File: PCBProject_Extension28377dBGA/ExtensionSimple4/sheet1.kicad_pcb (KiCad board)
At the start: 4 copper layers, 153.2 x 142.2 mm, 353 parts, among them J1 Conn_02x05_Odd_Even, J2 Conn_02x05_Odd_Even, J3 Conn_02x05_Odd_Even, J4 Conn_02x05_Odd_Even, Q1 FMMT618TA, U1 SN74ABT541, U2 SN74ABT541, U3 SN74ABT541, U4 SN74ABT541, U5 ADR423ARZ

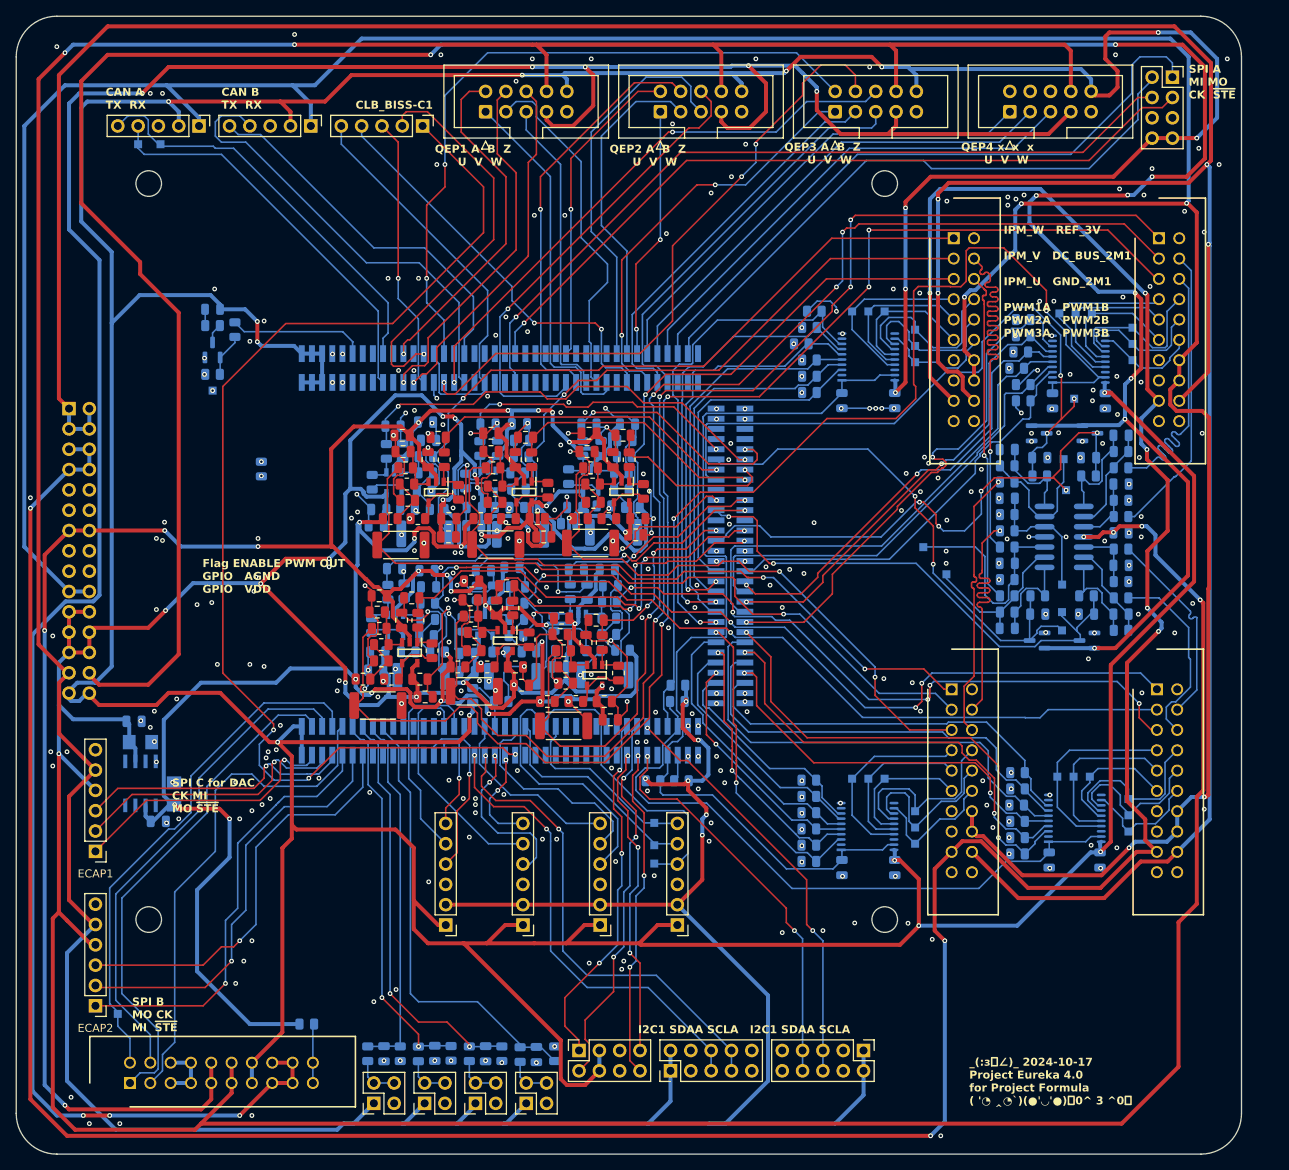
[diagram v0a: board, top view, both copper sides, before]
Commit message: waiting for improving quality of current sensor signals
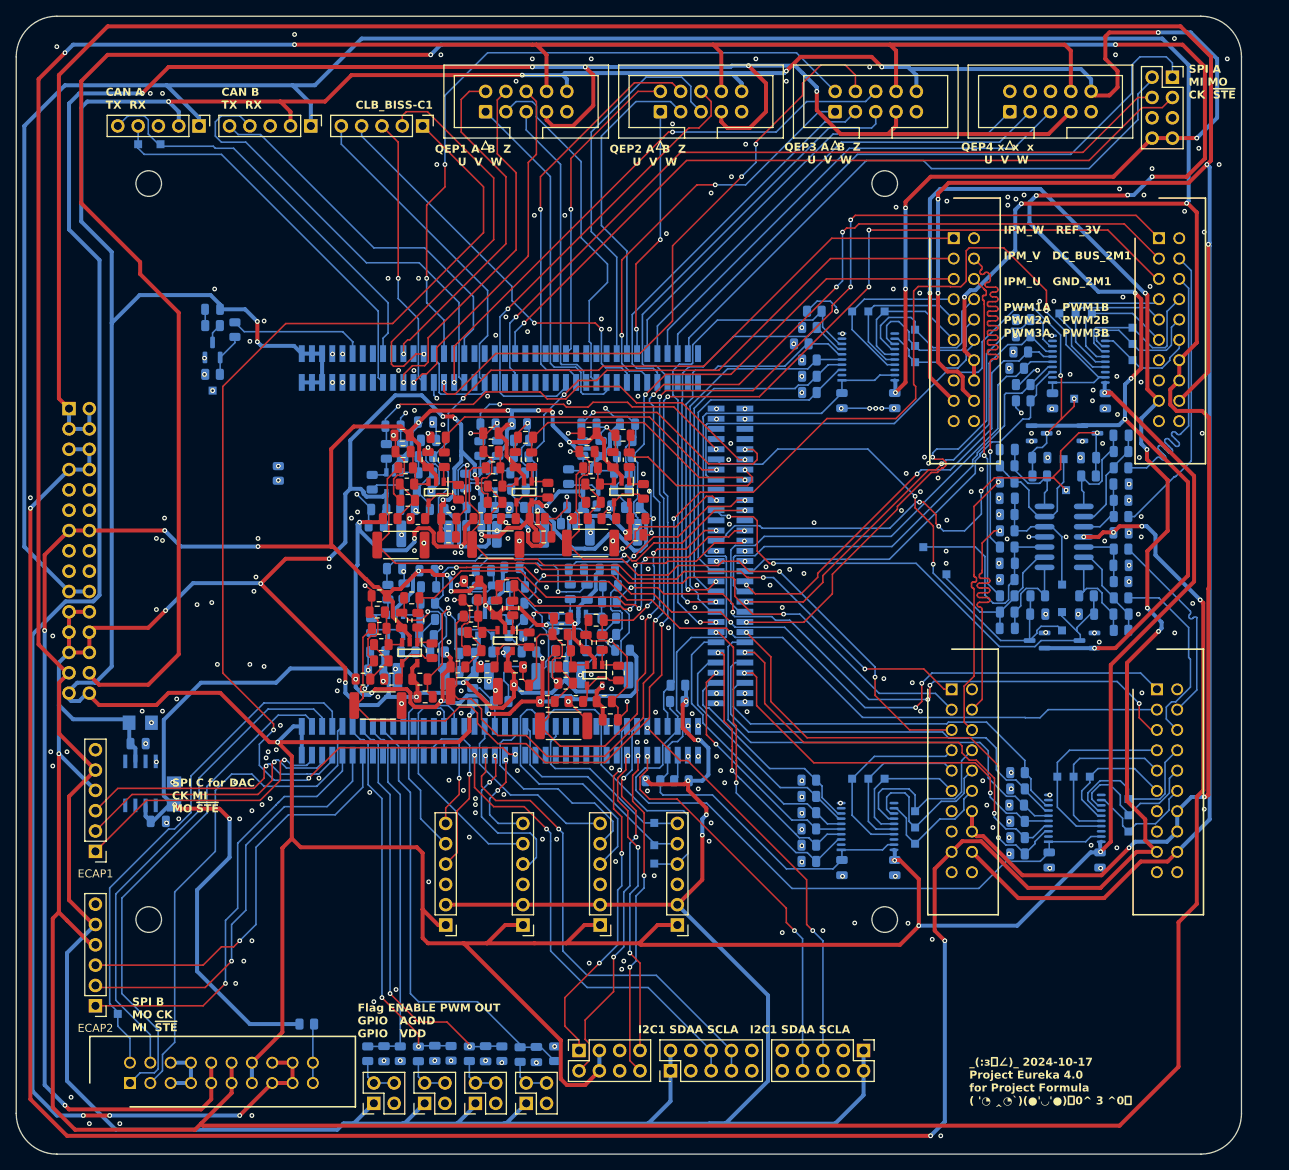
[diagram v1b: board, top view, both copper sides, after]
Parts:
- moved C23 2.84 mm to (190.0, 136.7)
- moved C25 2.43 mm to (188.9, 134.0)
- moved RU1 2.19 mm to (207.5, 102.9)
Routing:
- net REF_3V: track 249.8 -> 247.3 mm
- net D+5V: track 731.3 -> 729.3 mm
- net /IPM_VDC_BUS1: track 69.0 -> 68.1 mm
- net D12V1: track 411.9 -> 411.3 mm
- net AGND: vias 317 -> 323
- net 12VGND: vias 50 -> 51
